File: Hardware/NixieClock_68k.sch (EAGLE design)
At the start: 38 parts, among them IC1 68008, IC10 74HC32N, IC3 39SF020, IC4 DS1244Y, IC5 FT245R, IC6 NE555, IC7 74HC137N, IC8 74HC32N, IC9 74HC04N

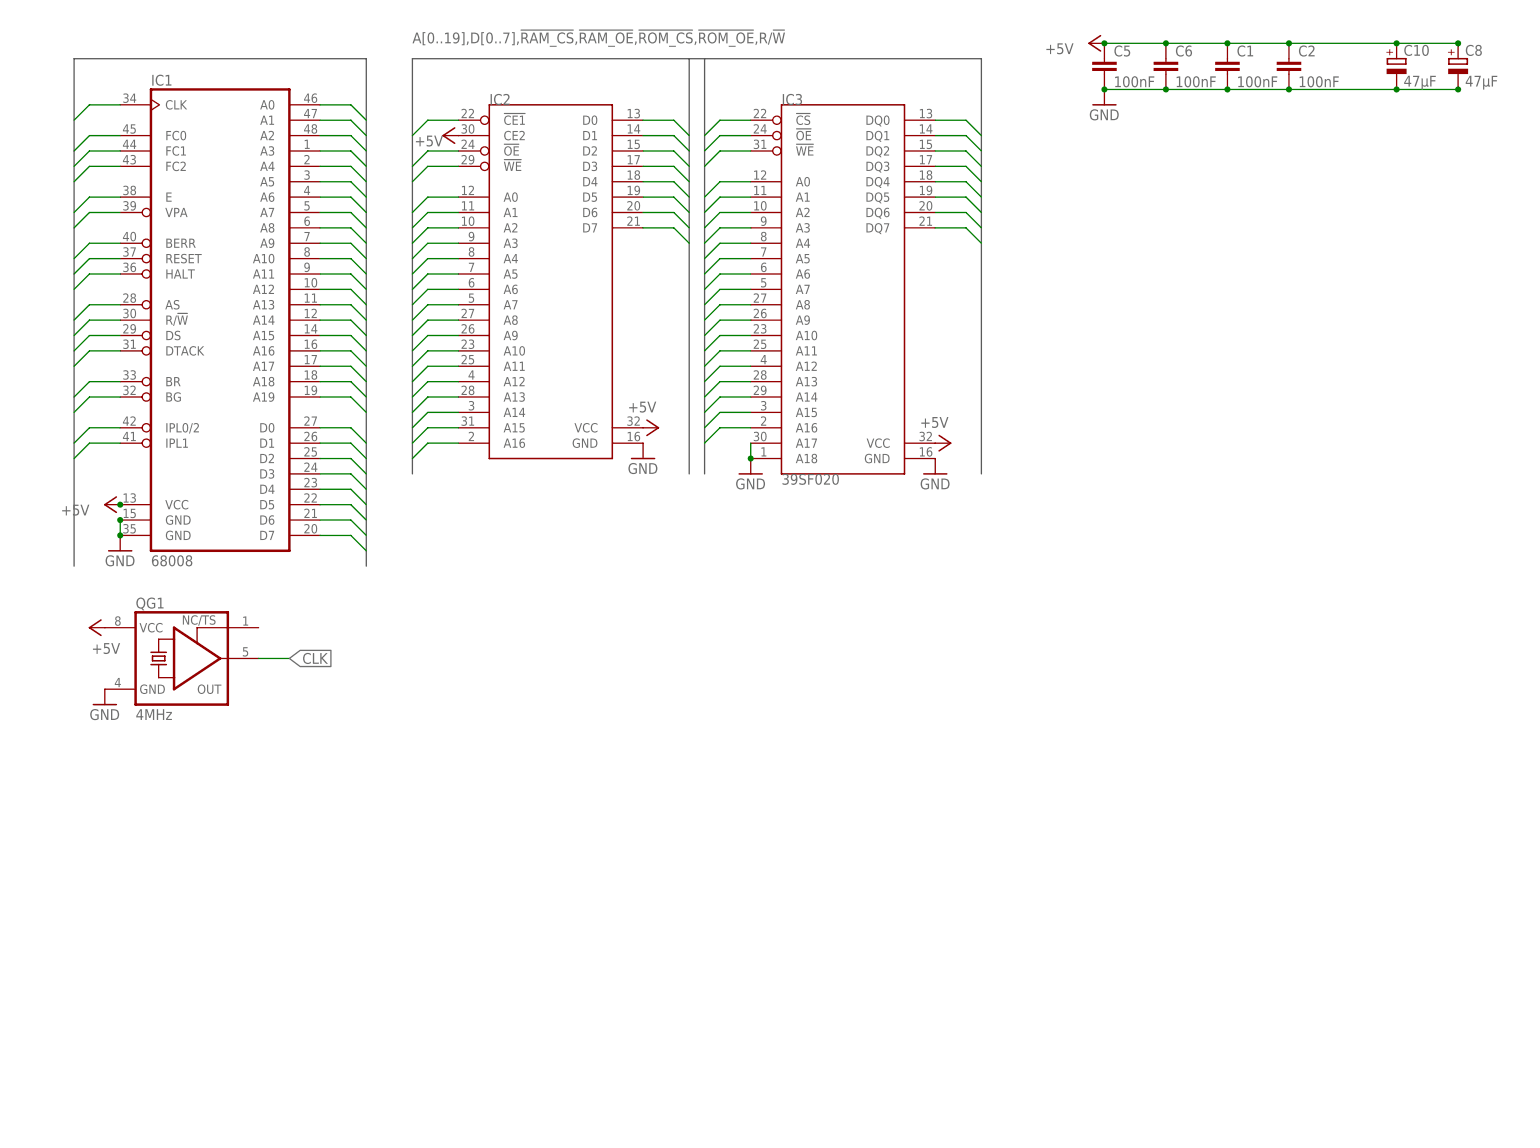
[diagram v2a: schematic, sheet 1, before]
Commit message: use cpld for all system logic
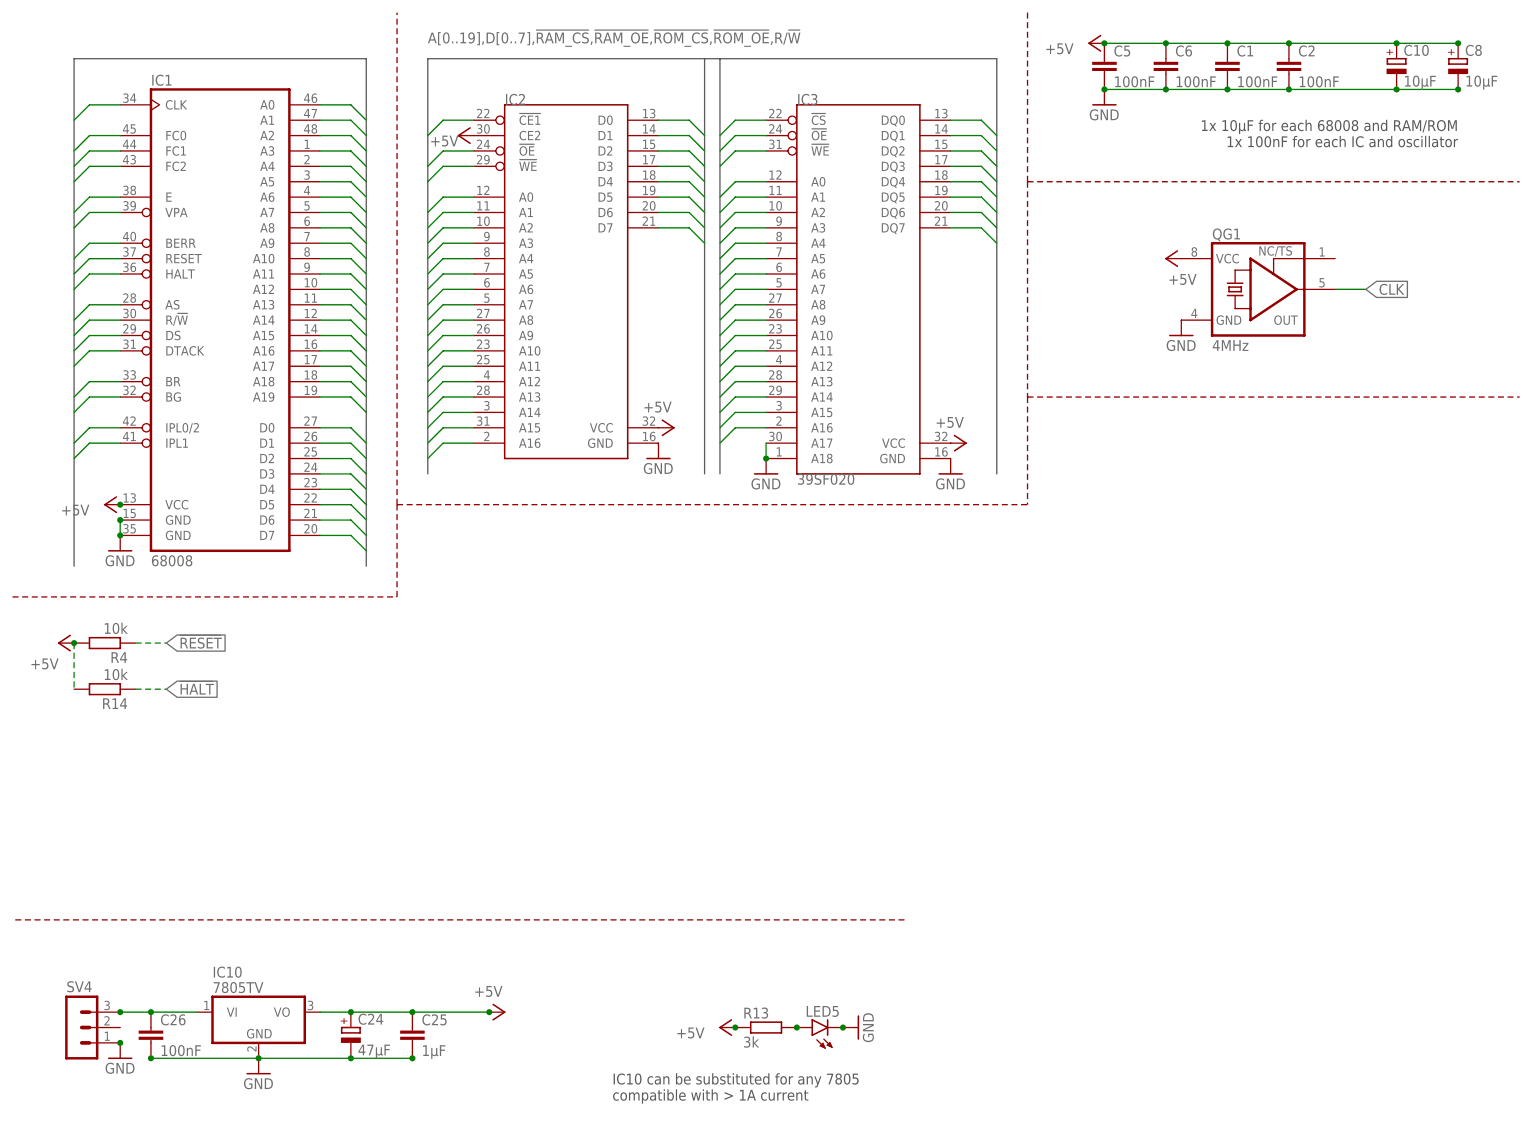
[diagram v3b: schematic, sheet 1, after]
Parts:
- added C22, C23, C26: 100nF, rcl:C-EUC0805
- added C24: 47µF, rcl:CPOL-EUCT6032
- added C25: 1µF, rcl:C-EUC0805
- added LED1, LED2, LED3, LED4, LED5: (no value), led:LEDCHIPLED_1206
- added R10, R11, R12, R14, R9: 10k, rcl:R-EU_R2012
- added R13, R5, R6, R7, R8: 3k, rcl:R-EU_R2012
- added SV3: (no value), con-lstb:MA05-2
- added SV4: (no value), con-lstb:MA03-1
- added SW1: (no value), special:SW_DIP-4
- C10, C14, C20, C4, C8: value 47µF -> 10µF; device rcl:CPOL-EUCT6032 -> rcl:CPOL-EUSMCB; MOUSER 581-TAJD476M016RNJV -> 581-TAJB106K020RNJV
- C18: MOUSER (none) -> 710-885342207010
- C19: MOUSER (none) -> 710-885012207096
- IC10: value 74HC32N -> 7805TV; device 74xx-eu:74HC32N -> linear:7805TV; MOUSER (none) -> 490-VXO7805-1000
- IC6: MOUSER (none) -> 595-NE555P
- IC7: value 74HC137N -> ATF1504AS; device 74xx-eu:74HC137N -> Parts:ATF1504ASPLCC44-SOCKET
- IC8: value 74HC32N -> 74HC377N; device 74xx-eu:74HC32N -> 74xx-eu:74HC377N; MOUSER (none) -> 595-SN74HC377N
- IC9: value 74HC04N -> 74HC373N; device 74xx-eu:74HC04N -> 74xx-eu:74HC373N; MOUSER (none) -> 595-SN74HC373N
- R1: MOUSER (none) -> 652-CR0805FX-1002ELF
- R2: MOUSER (none) -> 652-CR0805-JW-472ELF
- R3: MOUSER (none) -> 652-CR0805FX-1503ELF
- R4: value 0R -> 10k; MOUSER (none) -> 652-CR0805FX-1002ELF
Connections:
- removed net !A15: IC8B.I1, IC9A.O
- removed net !IO_CS: IC8B.O
- removed net !NIXIE_IO_CS: IC7A.Y4, IC8A.I0, IC8B.I0
- removed net !R!/W: IC8D.I1, IC9B.O
- removed net !RAM_CS_0: IC7A.Y6
- removed net !RAM_CS_1: IC7A.Y7
- removed net !ROM_CS_0: IC7A.Y0
- removed net !ROM_CS_1: IC7A.Y1
- removed net !USB_CS: IC7A.Y2, IC8C.I0, IC8D.I0
- removed net !USB_WR: IC8C.O, IC9C.I
- removed net !VFD_CS: IC10A.I0, IC7A.Y5
- new net !IO_IN_OE: IC7.IO24, IC9A.OC
- new net !IO_OUT_EN: IC8A.G
- new net !IO_OUT_RST: IC7.IO25
- new net !USB_RESET: IC5.!RESET, IC8A.8Q
- new net !VFD_RESET: IC8A.7Q, SV2.4
- new net CFG0: IC9A.5D, R9.1, SW1.5
- new net CFG1: IC9A.6D, R10.1, SW1.6
- new net CFG2: IC9A.7D, R11.1, SW1.7
- new net CFG3: IC9A.8D, R12.1, SW1.8
- new net CPLD_TCK: SV3.1
- new net CPLD_TDI: SV3.9
- new net CPLD_TDO: SV3.3
- new net CPLD_TMS: SV3.5
- new net JTAG_TCK: IC7.TCK
- new net JTAG_TDI: IC7.TDI
- new net JTAG_TDO: IC7.TDO
- new net JTAG_TMS: IC7.TMS
- new net N$3: LED1.A, R5.2
- new net N$4: LED5.A, R13.2
- new net N$5: LED2.A, R6.2
- new net N$7: LED3.A, R7.2
- new net N$8: C26.1, IC10.VI, SV4.3
- new net N$9: LED4.A, R8.2
- new net STATUS0: IC8A.1Q, R5.1
- new net STATUS1: IC8A.2Q, R6.1
- new net STATUS2: IC8A.3Q, R7.1
- new net STATUS3: IC8A.4Q, R8.1
- net !AS: now also IC7.IN1; no longer IC7A.G2, R4.2
- net !DTACK: now also IC7.IO18; no longer R4.1
- net !HALT: now also IC7.IO21, R14.1
- net !IPL0/2: now also IC7.IO19
- net !IPL1: now also IC7.IO11
- net !NIXIE_CS: now also IC7.IO31; no longer IC8A.O
- net !RAM_OE: now also IC7.IO36, IC7.IO37
- net !RESET: now also IC7.IO20, R4.1; no longer IC5.!RESET, SV2.4
- net !ROM_CS: now also IC7.IO40
- net !ROM_OE: now also IC7.IO39
- net !RTC_CS: now also IC7.IO34; no longer IC7A.Y3
- net !USB_RD: now also IC7.IO28; no longer IC8D.O
- net !USB_RXF: now also IC7.IO26, IC9A.3D
- net !USB_TXE: now also IC7.IO27, IC9A.2D
- net !VFD_WR: now also IC7.IO33; no longer IC10A.O
- net !VPA: now also IC7.IO12
- net +5V: now also C22.1, C23.1, C24.+, C25.1, IC10.VO, IC7.VCC, IC9A.ENC, R10.2, R11.2, R12.2, R13.1, R14.2, R4.2, R9.2, SV3.4; no longer IC10P.VCC, IC7A.G1, IC7P.VCC
- net A15: now also IC7.IO4; no longer IC8A.I1, IC9A.I
- net A16: now also IC7.IO5; no longer IC7A.A
- net A17: now also IC7.IO6; no longer IC7A.B
- net A18: now also IC7.IO8; no longer IC7A.C
- net CLK: now also IC7.GCLK1, IC8A.CLK
- net D0: now also IC8A.1D, IC9A.1Q
- net D1: now also IC8A.2D, IC9A.2Q
- net D2: now also IC8A.3D, IC9A.3Q
- net D3: now also IC8A.4D, IC9A.4Q
- net D4: now also IC8A.5D, IC9A.5Q
- net D5: now also IC8A.6D, IC9A.6Q
- net D6: now also IC8A.7D, IC9A.7Q
- net D7: now also IC8A.8D, IC9A.8Q
- net FC0: now also IC7.IO14
- net FC1: now also IC7.IO16
- net FC2: now also IC7.IO17
- net GND: now also C22.2, C23.2, C24.-, C25.2, C26.2, IC10.GND, IC7.GND, LED1.C, LED2.C, LED3.C, LED4.C, LED5.C, SV3.10, SV4.1, SW1.1, SW1.2, SW1.3, SW1.4; no longer IC10P.GND, IC7A.GL, IC7P.GND
- net R/!W!: now also IC7.IO9; no longer IC10A.I1, IC8C.I1, IC9B.I
- net TIMER_IRQ: now also IC7.IO41
- net USB_WR: now also IC7.IO29; no longer IC9C.O
- net VFD_BUSY: now also IC9A.1D
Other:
- note added: "1x 100nF per 74HCxxx"
- note added: "1x 10µF for VFD/Nixie connector 1x 10µF for FT245R/DS1244Y 1x 100nF for each IC and connector"
- note added: "1x 10µF for each 68008 and RAM/ROM 1x 100nF for each IC and oscillator"
- note added: "4x 100nF for ATF1504 1x 100nF for 555 1x 100nF for JTAG connector"
- note added: "IC10 can be substituted for any 7805 compatible with > 1A current"
- note added: "SV3: CPLD JTAG (Altera USB Blaster pinout)"
- note removed: "1x 100nF per 74xxx chip"
- note removed: "Zero waitstates for all memory OK up to 4MHz clock"
- moved on the sheet: C11, C13, C15, C16, C17, C21, C3, C7, C9, IC2, IC3, IC8P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

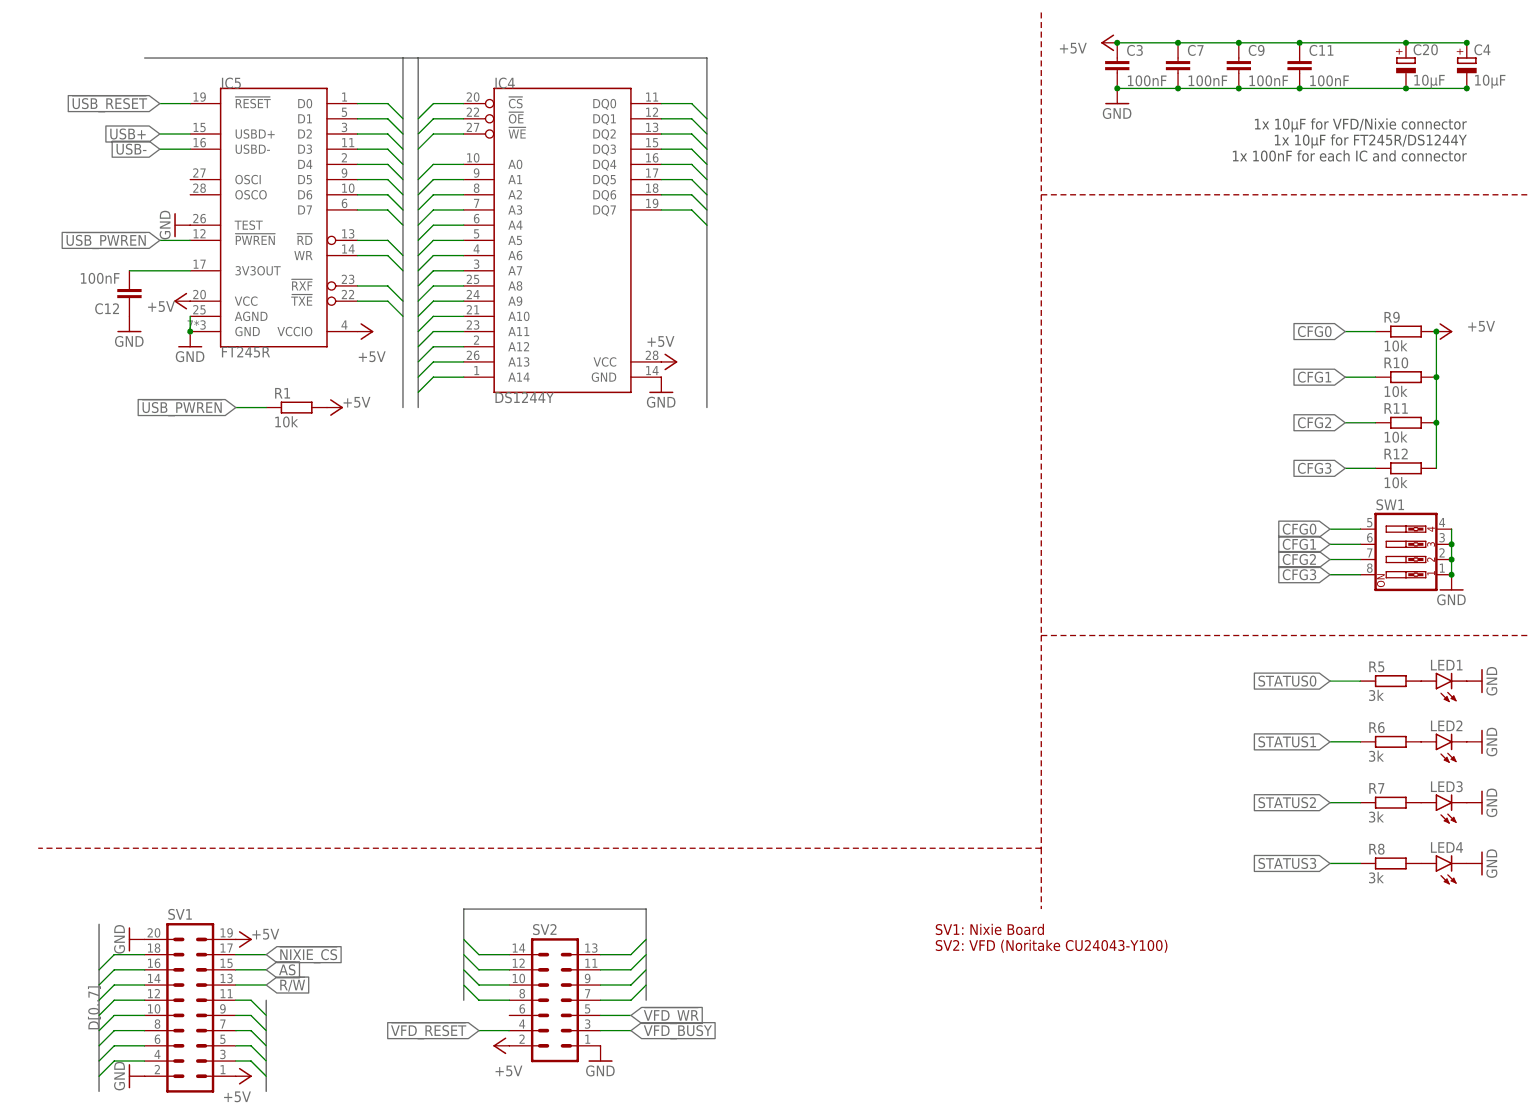
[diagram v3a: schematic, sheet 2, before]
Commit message: replaced SRAM with DIP variant
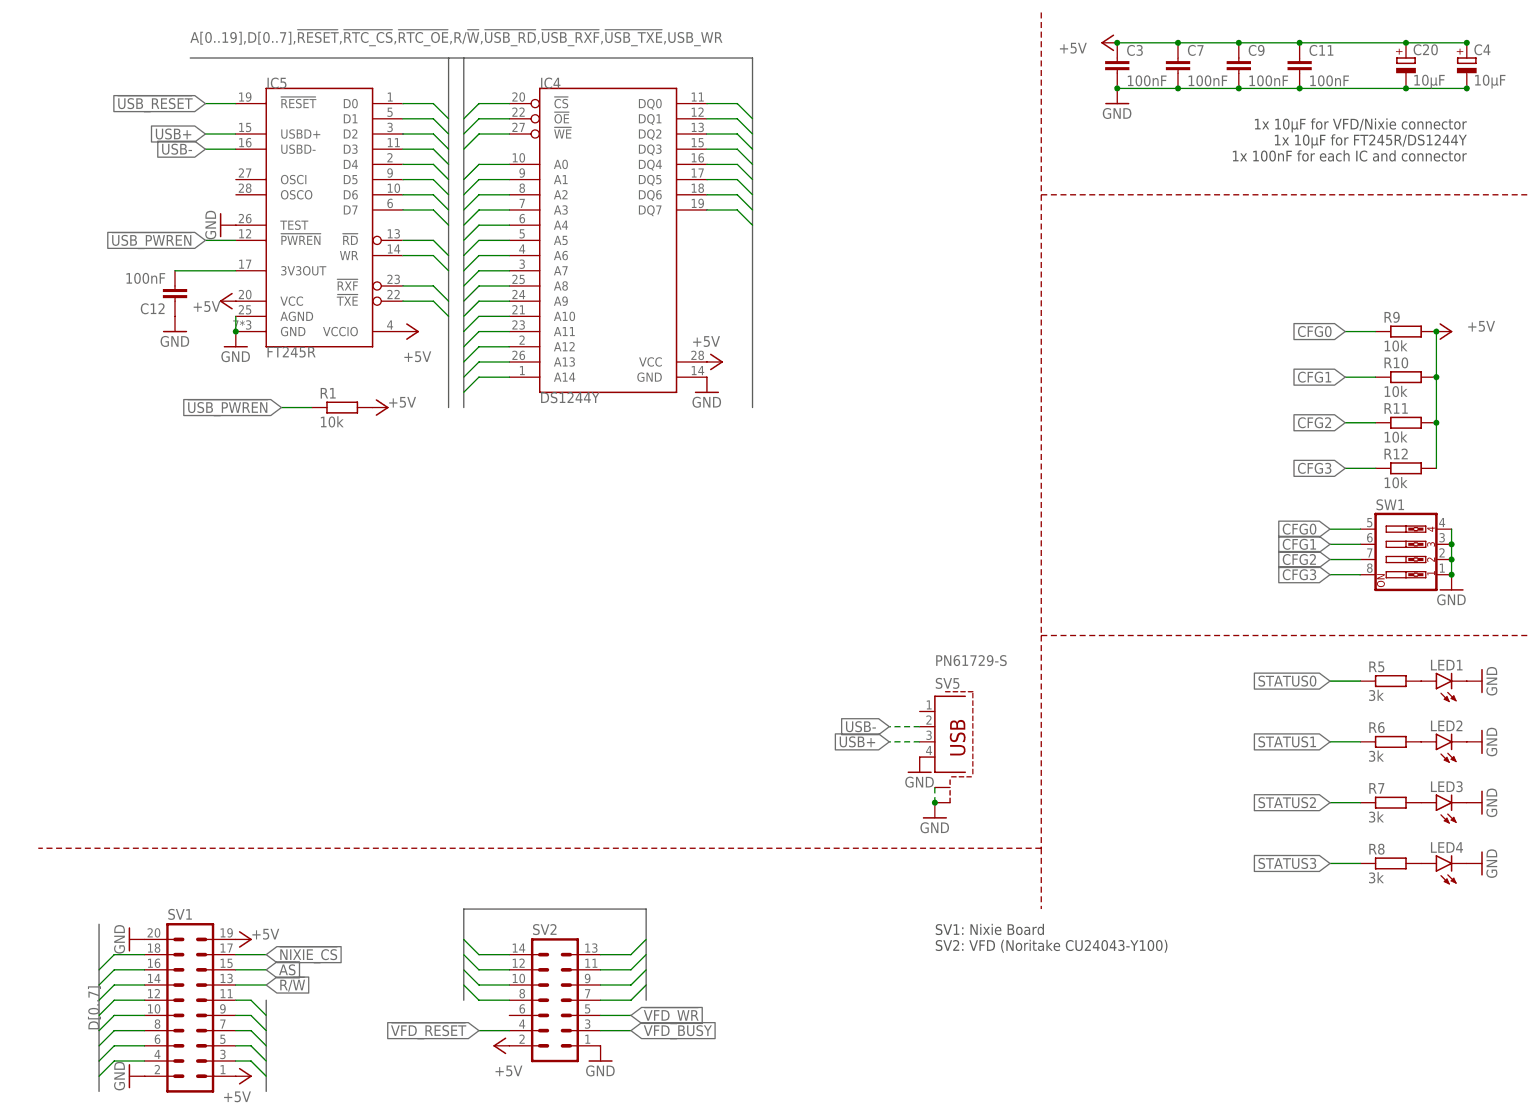
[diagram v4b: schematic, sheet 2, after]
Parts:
- added C27: 100nF, rcl:C-EUC0805
- added IC11: MIC803, Parts:MIC803SOT23-3
- added LED6: (no value), led:LEDCHIPLED_1206
- added R15, R16, R17, R18: 10k, rcl:R-EU_R2012
- added R19: 3k, rcl:R-EU_R2012
- added S1: (no value), switch-omron:10-XX
- added SV5: PN61729-S, con-berg:PN61729-S
- IC10: value 7805TV -> 7805
- IC2: value (none) -> AS6C1008; device Parts:CY62128BSOIC32 -> Parts:AS6C1008
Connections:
- removed net !HALT: IC1.HALT, IC7.IO21, R14.1
- new net BEEPER: IC8A.6Q
- new net N$6: LED6.A, R19.2
- net !BERR: now also R14.1
- net !BR: now also R18.1
- net !DS: now also IC7.IN44
- net !RESET: now also IC1.HALT, IC11.!RESET, LED6.C, S1.S, S1.S1
- net +5V: now also C27.1, IC11.VCC, R15.2, R16.2, R18.2, R19.1
- net CPLD_TCK: now also R17.1
- net CPLD_TDI: now also R16.1
- net CPLD_TMS: now also R15.1
- net GND: now also C27.2, IC11.GND, R17.2, S1.P, S1.P1, SV5.4, SV5.S1, SV5.S2
- net USB+: now also SV5.3
- net USB-: now also SV5.2
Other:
- note added: "1x 10µF for each 68008 and RAM/ROM 1x 100nF for each IC and oscillator 1x 100nF for PoR monitor"
- note added: "S1: reset switch"
- note removed: "1x 10µF for each 68008 and RAM/ROM 1x 100nF for each IC and oscillator"
- moved on the sheet: C10, C12, C8, IC4, IC5, R1

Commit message: start board layout
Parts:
- added D1: 1N4148, diode:1N4148DO35-7
- added Q1: 2N4401, transistor-npn:2N4416
- added R20: 4k7, rcl:R-EU_R2012
- added R21, R22, R23: 10k, rcl:R-EU_R2012
- added R24, R25: 1k, rcl:R-EU_R2012
- added SP1: KSS1201, buzzer:KSS1201
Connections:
- net !IO_IN_OE renamed !IO_IN_CS
- removed net !IO_OUT_RST: IC7.IO25
- removed net !RAM_OE: IC2.!OE, IC7.IO36, IC7.IO37
- removed net !ROM_OE: IC3.!OE, IC7.IO39
- removed net !RTC_OE: IC4.!OE
- new net !IO_OUT_CS: IC8A.G
- new net !OE: IC2.!OE, IC3.!OE, IC4.!OE, IC7.IO39
- new net N$10: R20.2, SV5.1
- new net N$11: Q1.B, R24.2
- new net N$12: D1.A, Q1.C, SP1.2
- new net N$13: D1.C, R25.1
- new net VPA: R22.1
- net !DTACK: now also IC7.IO20, R23.1; no longer IC7.IO18
- net !IO_OUT_EN: now also IC7.IO25; no longer IC8A.G
- net !IPL0/2: now also IC7.IO14; no longer IC7.IO19
- net !IPL1: now also IC7.IO12; no longer IC7.IO11
- net !RAM_CS: now also IC7.IO36
- net !RESET: now also IC7.IO21; no longer IC7.IO20
- net !ROM_CS: now also IC7.IO37; no longer IC7.IO40
- net !USB_RESET: now also R20.1, R21.2; no longer IC8A.8Q
- net !VFD_RESET: now also IC8A.8Q; no longer IC8A.7Q
- net !VPA: now also IC7.IO16; no longer IC7.IO12
- net +5V: now also R22.2, R23.2, R25.2, SP1.1
- net A19: now also IC7.IO9
- net BEEPER: now also IC8A.7Q, R24.1; no longer IC8A.6Q
- net FC0: now also IC7.IO17; no longer IC7.IO14
- net FC1: now also IC7.IO18; no longer IC7.IO16
- net FC2: now also IC7.IO19; no longer IC7.IO17
- net GND: now also Q1.E, R21.1
- net R/!W!: now also IC7.IO11; no longer IC7.IO9
